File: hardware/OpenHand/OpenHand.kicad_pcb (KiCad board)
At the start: 4 copper layers, 110 x 50 mm, 271 parts, among them J1 CONN_MOTOR_1, J10 CONN_JTAG, J11 CONN_FDBK_2, J12 CONN_EMG_2, J13 CONN_POS_3, J2 CONN_MOTOR_2, J3 CONN_BATT, J4 USB_C_CONN, J5 CONN_POS_1, J6 CONN_MOTOR_3, J7 CONN_FDBK_1, J8 CONN_EMG_1, J9 CONN_POS_2, Q1 2N7002, Q2 2N7002, Q3 PMOS, SW1 SW_Push, SW2 BTN_RST, SW3 BTN_BOOT, U1 CH340C, U10 DRV8833PWP, U11 DRV8833PWP, U12 DRV8833PWP, U13 DRV8833PWP, U14 ESP32-S3-WROOM-1, U2 STM32F103RETx, U3 TPS63070RNMR, U4 AMS1117-3.3, U5 LT1175-5_SOT223, U6 LM324, U7 LM324, U8 ADS1115IDGS, U9 ADS1115IDGS

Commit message: Major updates to schm and pcb, a bit better design
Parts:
- removed the J4 at (104.2, 114.4)
- removed JP17, JP18: SolderJumper_2_Open, Jumper:SolderJumper-2_P1.3mm_Open_RoundedPad1.0x1.5mm
- removed JP19: JMPR_BTN_1, Jumper:SolderJumper-2_P1.3mm_Bridged_RoundedPad1.0x1.5mm
- removed JP20: JMPR_LED_2, Jumper:SolderJumper-2_P1.3mm_Bridged_RoundedPad1.0x1.5mm
- removed JP21: JMPR_BTN_RST, Jumper:SolderJumper-2_P1.3mm_Bridged_RoundedPad1.0x1.5mm
- removed JP22: JMPR_BTN_BOOT, Jumper:SolderJumper-2_P1.3mm_Bridged_RoundedPad1.0x1.5mm
- removed JP23: JMPR_REVP, Jumper:SolderJumper-2_P1.3mm_Bridged_RoundedPad1.0x1.5mm
- removed JP24: JMPR_PSU, Jumper:SolderJumper-2_P1.3mm_Bridged_RoundedPad1.0x1.5mm
- removed JP25: JMPR_EMG_2_UC, Jumper:SolderJumper-2_P1.3mm_Bridged_RoundedPad1.0x1.5mm
- removed JP26: JMPR_EMG_1_UC, Jumper:SolderJumper-2_P1.3mm_Bridged_RoundedPad1.0x1.5mm
- removed JP27: JMPR_I2C_ADC_SCL, Jumper:SolderJumper-2_P1.3mm_Bridged_RoundedPad1.0x1.5mm
- removed JP28: JMPR_I2C_ADC_SDA, Jumper:SolderJumper-2_P1.3mm_Bridged_RoundedPad1.0x1.5mm
- removed JP29: JMPR_MOT_1_EN, Jumper:SolderJumper-2_P1.3mm_Bridged_RoundedPad1.0x1.5mm
- removed JP30: JMPR_MOT_2_EN, Jumper:SolderJumper-2_P1.3mm_Bridged_RoundedPad1.0x1.5mm
- removed JP31: JMPR_MOT_1_UC1, Jumper:SolderJumper-2_P1.3mm_Bridged_RoundedPad1.0x1.5mm
- removed JP32: JMPR_MOT_2_UC1, Jumper:SolderJumper-2_P1.3mm_Bridged_RoundedPad1.0x1.5mm
- removed JP33: JMPR_MOT_1_UC2, Jumper:SolderJumper-2_P1.3mm_Bridged_RoundedPad1.0x1.5mm
- removed JP34: JMPR_MOT_2_UC2, Jumper:SolderJumper-2_P1.3mm_Bridged_RoundedPad1.0x1.5mm
- removed JP35: JMPR_MOT_3_EN, Jumper:SolderJumper-2_P1.3mm_Bridged_RoundedPad1.0x1.5mm
- removed JP36: JMPR_MOT_3_UC1, Jumper:SolderJumper-2_P1.3mm_Bridged_RoundedPad1.0x1.5mm
- removed JP37: JMPR_MOT_3_UC2, Jumper:SolderJumper-2_P1.3mm_Bridged_RoundedPad1.0x1.5mm
- removed JP38: JMPR_ESP_USB_P, Jumper:SolderJumper-2_P1.3mm_Bridged_RoundedPad1.0x1.5mm
- removed JP39: JMPR_ESP_USB_N, Jumper:SolderJumper-2_P1.3mm_Bridged_RoundedPad1.0x1.5mm
- removed JP40: JMPR_ESP_SCL, Jumper:SolderJumper-2_P1.3mm_Bridged_RoundedPad1.0x1.5mm
- removed JP41: JMPR_ESP_SDA, Jumper:SolderJumper-2_P1.3mm_Bridged_RoundedPad1.0x1.5mm
- removed Q2: 2N7002, Package_TO_SOT_SMD:SOT-23
- removed Q3: PMOS, Package_DIP:Vishay_HVM-DIP-3_W7.62mm
- removed R61: 10k, Resistor_SMD:R_1206_3216Metric_Pad1.30x1.75mm_HandSolder
- removed R62, R64: 4R7, Resistor_SMD:R_1206_3216Metric_Pad1.30x1.75mm_HandSolder
- removed R63: 0R2, Resistor_SMD:R_1206_3216Metric_Pad1.30x1.75mm_HandSolder
- removed TP57: TP_MOT_2_IS, TestPoint:TestPoint_Pad_D1.0mm
- removed TP58: TP_MOT_2_FAULT, TestPoint:TestPoint_Pad_D1.0mm
- removed TP59: TP_MOT_1_UC1, TestPoint:TestPoint_Pad_D1.0mm
- removed TP60: TP_MOT_2_UC1, TestPoint:TestPoint_Pad_D1.0mm
- removed TP61: TP_MOT_1_UC2, TestPoint:TestPoint_Pad_D1.0mm
- removed TP62: TP_MOT_2_UC2, TestPoint:TestPoint_Pad_D1.0mm
- removed TP63: TP_MOT_1_OUT_P, TestPoint:TestPoint_Pad_D1.0mm
- removed TP64: TP_MOT_2_OUT_P, TestPoint:TestPoint_Pad_D1.0mm
- removed TP65: TP_MOT_1_OUT_N, TestPoint:TestPoint_Pad_D1.0mm
- removed TP66: TP_MOT_2_OUT_N, TestPoint:TestPoint_Pad_D1.0mm
- removed TP67: TP_MOT_3_EN, TestPoint:TestPoint_Pad_D1.0mm
- removed TP68: TP_FDBK_MOT_EN, TestPoint:TestPoint_Pad_D1.0mm
- removed TP69: TP_MOT_3_IS, TestPoint:TestPoint_Pad_D1.0mm
- removed TP70: TP_MOT_3_FAULT, TestPoint:TestPoint_Pad_D1.0mm
- removed TP71: TP_FDBK_MOT_FAULT, TestPoint:TestPoint_Pad_D1.0mm
- removed TP72: TP_MOT_3_UC1, TestPoint:TestPoint_Pad_D1.0mm
- removed TP73: TP_FDBK_MOT_1_UC1, TestPoint:TestPoint_Pad_D1.0mm
- removed TP74: TP_MOT_3_UC2, TestPoint:TestPoint_Pad_D1.0mm
- removed TP75: TP_FDBK_MOT_1_UC2, TestPoint:TestPoint_Pad_D1.0mm
- removed TP76: TP_MOT_3_OUT_P, TestPoint:TestPoint_Pad_D1.0mm
- removed TP77: TP_MOT_3_OUT_N, TestPoint:TestPoint_Pad_D1.0mm
- removed TP78: TP_FDBK_MOT_2_UC1, TestPoint:TestPoint_Pad_D1.0mm
- removed TP79: TP_FDBK_MOT_2_UC2, TestPoint:TestPoint_Pad_D1.0mm
- removed TP80: TP_ESP_SCL, TestPoint:TestPoint_Pad_D1.0mm
- removed TP81: TP_ESP_SDA, TestPoint:TestPoint_Pad_D1.0mm
- removed U11, U12, U13: DRV8833PWP, Package_SO:HTSSOP-16-1EP_4.4x5mm_P0.65mm_EP3.4x5mm_Mask2.46x2.31mm_ThermalVias
- removed U14: ESP32-S3-WROOM-1, Espressif:ESP32-S3-WROOM-1
- added C39: 10u, Capacitor_SMD:C_0805_2012Metric, F.Cu at (181.2, 122.0)
- added J5: USB_C_CONN, Connector_USB:USB_C_Receptacle_G-Switch_GT-USB-7010ASV, F.Cu at (104.0, 114.1)
- added TP39: TP_MOT_2_UC2, TestPoint:TestPoint_Pad_D1.0mm, B.Cu at (145.9, 117.1)
- added TP40: TP_MOT_1_OUT_P, TestPoint:TestPoint_Pad_D1.0mm, F.Cu at (176.1, 137.7)
- C1: value 1u -> 100n; footprint Capacitor_SMD:C_1206_3216Metric_Pad1.33x1.80mm_HandSolder -> Capacitor_SMD:C_0805_2012Metric
- C10, C5, C9: value 10u -> 100n; footprint Capacitor_SMD:C_0805_2012Metric_Pad1.18x1.45mm_HandSolder -> Capacitor_SMD:C_0805_2012Metric
- C11: value 10u -> 22u; footprint Capacitor_SMD:C_0805_2012Metric_Pad1.18x1.45mm_HandSolder -> Capacitor_SMD:C_0805_2012Metric
- C12, C15: value 100n -> 22u; footprint Capacitor_SMD:C_1206_3216Metric_Pad1.33x1.80mm_HandSolder -> Capacitor_SMD:C_0805_2012Metric
- C13: value 22u -> 1u; footprint Capacitor_SMD:C_0805_2012Metric_Pad1.18x1.45mm_HandSolder -> Capacitor_SMD:C_0805_2012Metric
- C14, C18, C19, C20, C21, C22, C24, C26, C28, C30, C32, C34, C36, C38: footprint Capacitor_SMD:C_0805_2012Metric_Pad1.18x1.45mm_HandSolder -> Capacitor_SMD:C_0805_2012Metric
- C16, C2, C3, C4: footprint Capacitor_SMD:C_1206_3216Metric_Pad1.33x1.80mm_HandSolder -> Capacitor_SMD:C_0805_2012Metric
- C17: value 470n -> 100n; footprint Capacitor_SMD:C_0805_2012Metric_Pad1.18x1.45mm_HandSolder -> Capacitor_SMD:C_0805_2012Metric
- C23: value 330n -> 470n; footprint Capacitor_SMD:C_0805_2012Metric_Pad1.18x1.45mm_HandSolder -> Capacitor_SMD:C_0805_2012Metric
- C25: value 10u -> 330n; footprint Capacitor_SMD:C_0805_2012Metric_Pad1.18x1.45mm_HandSolder -> Capacitor_SMD:C_0805_2012Metric
- C27, C33: value 2u2 -> 10u; footprint Capacitor_SMD:C_0805_2012Metric_Pad1.18x1.45mm_HandSolder -> Capacitor_SMD:C_0805_2012Metric
- C29, C35: value 10n -> 2u2; footprint Capacitor_SMD:C_0805_2012Metric_Pad1.18x1.45mm_HandSolder -> Capacitor_SMD:C_0805_2012Metric
- C31, C37: value 10u -> 10n; footprint Capacitor_SMD:C_0805_2012Metric_Pad1.18x1.45mm_HandSolder -> Capacitor_SMD:C_0805_2012Metric
- C6: value 22u -> 100n; footprint Capacitor_SMD:C_0805_2012Metric_Pad1.18x1.45mm_HandSolder -> Capacitor_SMD:C_0805_2012Metric
- C7, C8: value 22u -> 10u; footprint Capacitor_SMD:C_0805_2012Metric_Pad1.18x1.45mm_HandSolder -> Capacitor_SMD:C_0805_2012Metric
- D1, D2, D4: footprint LED_SMD:LED_0805_2012Metric -> LED_SMD:LED_1210_3225Metric
- D3: footprint Diode_THT:D_A-405_P7.62mm_Horizontal -> Diode_SMD:D_SOD-123
- JP1: value JMPR_RST -> JMPR_TRIM_1
- JP14: value JMPR_LED_1 -> SolderJumper_2_Open; footprint Jumper:SolderJumper-2_P1.3mm_Bridged_RoundedPad1.0x1.5mm -> Jumper:SolderJumper-2_P1.3mm_Open_RoundedPad1.0x1.5mm; moved to B.Cu
- JP15: value SolderJumper_2_Open -> JMPR_EMG_1_UC; footprint Jumper:SolderJumper-2_P1.3mm_Open_RoundedPad1.0x1.5mm -> Jumper:SolderJumper-2_P1.3mm_Bridged_RoundedPad1.0x1.5mm; moved to F.Cu
- JP16: value SolderJumper_2_Open -> JMPR_EMG_2_UC; footprint Jumper:SolderJumper-2_P1.3mm_Open_RoundedPad1.0x1.5mm -> Jumper:SolderJumper-2_P1.3mm_Bridged_RoundedPad1.0x1.5mm; moved to F.Cu
- JP2: value JMPR_RX -> JMPR_LED_1
- JP3: value JMPR_TX -> JMPR_BTN_1
- JP4: value JMPR_USB_P -> JMPR_LED_2
- JP5: value JMPR_USB_N -> JMPR_TRIM_2
- JP6: value JMPR_BOOT -> JMPR_POT_1
- JP7: value JMPR_POT_1 -> SolderJumper_2_Open; footprint Jumper:SolderJumper-2_P1.3mm_Bridged_RoundedPad1.0x1.5mm -> Jumper:SolderJumper-2_P1.3mm_Open_RoundedPad1.0x1.5mm; moved to B.Cu
- JP8: value JMPR_TRIM_1 -> SolderJumper_2_Open; footprint Jumper:SolderJumper-2_P1.3mm_Bridged_RoundedPad1.0x1.5mm -> Jumper:SolderJumper-2_P1.3mm_Open_RoundedPad1.0x1.5mm; moved to B.Cu
- JP9: value JMPR_TRIM_2 -> SolderJumper_2_Open; footprint Jumper:SolderJumper-2_P1.3mm_Bridged_RoundedPad1.0x1.5mm -> Jumper:SolderJumper-2_P1.3mm_Open_RoundedPad1.0x1.5mm; moved to B.Cu
- L1: value 1.5uH -> 3.3uH; footprint Inductor_THT:L_Radial_D6.0mm_P4.00mm -> Inductor_SMD:L_Bourns_SRP7028A_7.3x6.6mm
- Q1: value 2N7002 -> AO3401A
- R1: value 5k1 -> 10k; footprint Resistor_SMD:R_0805_2012Metric_Pad1.20x1.40mm_HandSolder -> Resistor_SMD:R_0805_2012Metric
- R10, R9: value 10k -> 4k7; footprint Resistor_SMD:R_0805_2012Metric_Pad1.20x1.40mm_HandSolder -> Resistor_SMD:R_0805_2012Metric; moved to F.Cu
- R11: value 4k7 -> 47k; footprint Resistor_SMD:R_0805_2012Metric_Pad1.20x1.40mm_HandSolder -> Resistor_SMD:R_0805_2012Metric
- R12, R19, R2, R22, R25, R26, R27, R28, R29, R30, R31, R32, R33, R37, R38, R39, R40, R41, R42, R45, R46, R47, R48, R49, R5, R50, R51, R52, R53, R6: footprint Resistor_SMD:R_0805_2012Metric_Pad1.20x1.40mm_HandSolder -> Resistor_SMD:R_0805_2012Metric
- R13: value 4k7 -> 10k; footprint Resistor_SMD:R_0805_2012Metric_Pad1.20x1.40mm_HandSolder -> Resistor_SMD:R_0805_2012Metric; moved to B.Cu
- R14, R15, R16: footprint Resistor_SMD:R_0805_2012Metric_Pad1.20x1.40mm_HandSolder -> Resistor_SMD:R_0805_2012Metric; moved to B.Cu
- R17: value 680k -> 10k; footprint Resistor_SMD:R_0805_2012Metric_Pad1.20x1.40mm_HandSolder -> Resistor_SMD:R_0805_2012Metric
- R18: value 100k -> 54.9k; footprint Resistor_SMD:R_0805_2012Metric_Pad1.20x1.40mm_HandSolder -> Resistor_SMD:R_0805_2012Metric
- R20: value 130k -> 4k7; footprint Resistor_SMD:R_0805_2012Metric_Pad1.20x1.40mm_HandSolder -> Resistor_SMD:R_0805_2012Metric
- R21: value 4k7 -> 10k; footprint Resistor_SMD:R_0805_2012Metric_Pad1.20x1.40mm_HandSolder -> Resistor_SMD:R_0805_2012Metric
- R23: value 47k -> 15k; footprint Resistor_SMD:R_0805_2012Metric_Pad1.20x1.40mm_HandSolder -> Resistor_SMD:R_0805_2012Metric
- R24, R35: value 15k -> 47k; footprint Resistor_SMD:R_0805_2012Metric_Pad1.20x1.40mm_HandSolder -> Resistor_SMD:R_0805_2012Metric
- R3: value 1k -> 5k1; footprint Resistor_SMD:R_0805_2012Metric_Pad1.20x1.40mm_HandSolder -> Resistor_SMD:R_0805_2012Metric
- R34: value 47k -> 10k; footprint Resistor_SMD:R_0805_2012Metric_Pad1.20x1.40mm_HandSolder -> Resistor_SMD:R_0805_2012Metric
- R36: value 10k -> 15k; footprint Resistor_SMD:R_0805_2012Metric_Pad1.20x1.40mm_HandSolder -> Resistor_SMD:R_0805_2012Metric
- R4: value 1k -> 1.5k; footprint Resistor_SMD:R_0805_2012Metric_Pad1.20x1.40mm_HandSolder -> Resistor_SMD:R_0805_2012Metric
- R43: value 1k -> 47k; footprint Resistor_SMD:R_0805_2012Metric_Pad1.20x1.40mm_HandSolder -> Resistor_SMD:R_0805_2012Metric
- R44: value 47k -> 1k; footprint Resistor_SMD:R_0805_2012Metric_Pad1.20x1.40mm_HandSolder -> Resistor_SMD:R_0805_2012Metric
- R54: value 47k -> 0R2; footprint Resistor_SMD:R_0805_2012Metric_Pad1.20x1.40mm_HandSolder -> Resistor_SMD:R_1206_3216Metric
- R55: value 10k -> 0R2; footprint Resistor_SMD:R_0805_2012Metric_Pad1.20x1.40mm_HandSolder -> Resistor_SMD:R_1206_3216Metric
- R56, R57: footprint Resistor_SMD:R_1206_3216Metric_Pad1.30x1.75mm_HandSolder -> Resistor_SMD:R_0805_2012Metric
- R58: value 0R2 -> 4R7; footprint Resistor_SMD:R_1206_3216Metric_Pad1.30x1.75mm_HandSolder -> Resistor_SMD:R_1206_3216Metric
- R59: footprint Resistor_SMD:R_1206_3216Metric_Pad1.30x1.75mm_HandSolder -> Resistor_SMD:R_1206_3216Metric
- R60: value 10k -> 4R7; footprint Resistor_SMD:R_1206_3216Metric_Pad1.30x1.75mm_HandSolder -> Resistor_SMD:R_1206_3216Metric
- R7, R8: footprint Resistor_SMD:R_0805_2012Metric_Pad1.20x1.40mm_HandSolder -> Resistor_SMD:R_0805_2012Metric; moved to F.Cu
- RV1: value TRIM_POT_3 -> TRIM_POT_1
- RV2: value TRIM_POT_1 -> TRIM_POT_2
- RV3: value TRIM_POT_2 -> TRIM_POT_3
- SW1: value SW_Push -> BTN_RST
- SW2: value BTN_RST -> BTN_BOOT
- SW3: value BTN_BOOT -> SW_Push
- TP1: value TP_UC_RST -> TP_BTN_RST
- TP10: value TP_UC_RX -> TP_HALL_01
- TP11: value TP_LED_1 -> TP_HALL_02
- TP12: value TP_UC_TX -> TP_HALL_03
- TP13: value TP_HW_REV_3 -> TP_UC_TX; moved to F.Cu
- TP14: value TP_UC_PIN_PD1 -> TP_UC_RX; moved to F.Cu
- TP15: value TP_HW_REV_4 -> TP_UC_PIN_PC12; moved to F.Cu
- TP16: value TP_UC_PIN_PD2 -> TP_UC_SCL; moved to F.Cu
- TP17: value TP_UC_PIN_PC0 -> TP_UC_SDA; moved to F.Cu
- TP18: value TP_UC_PIN_PC1 -> TP_UC_PIN_PB12; moved to F.Cu
- TP19: value TP_LED_2 -> TP_BATT_P
- TP20: value TP_UC_PIN_PC2 -> TP_V_BATT; moved to F.Cu
- TP21: value TP_UC_PIN_PC3 -> TP_V_5V; moved to F.Cu
- TP22: value TP_UC_PIN_PB2 -> TP_V_3V3; moved to F.Cu
- TP23: value TP_UC_PIN_PC13 -> TP_V_N5V; moved to F.Cu
- TP24: value TP_UC_PIN_PB5 -> TP_EMG_1_AMP; moved to F.Cu
- TP25: value TP_UC_PIN_PC14 -> TP_EMG_2_AMP; moved to F.Cu
- TP26: value TP_UC_PIN_PC15 -> TP_EMG_1_HP; moved to F.Cu
- TP27: value TP_UC_PIN_PB10 -> TP_EMG_2_HP; moved to F.Cu
- TP28: value TP_UC_PIN_PB11 -> TP_EMG_1_LP; moved to F.Cu
- TP29: value TP_BATT_P -> TP_EMG_2_LP
- TP30: value TP_V_BATT -> TP_MOT_1_EN
- TP31: value TP_V_5V -> TP_MOT_2_EN
- TP32: value TP_PSU_FDBK -> TP_MOT_1_IS
- TP33: value TP_V_3V3 -> TP_MOT_1_FAULT
- TP34: value TP_V_N5V -> TP_MOT_2_IS
- TP35: value TP_EMG_2_AMP -> TP_MOT_2_FAULT
- TP36: value TP_EMG_1_AMP -> TP_MOT_1_UC1; moved to B.Cu
- TP37: value TP_EMG_2_HP -> TP_MOT_2_UC1; moved to B.Cu
- TP38: value TP_EMG_1_HP -> TP_MOT_1_UC2; moved to B.Cu
- TP4: value TP_UC_BOOT -> TP_BTN_BOOT
- TP41: value TP_EMG_2_LP -> TP_MOT_2_OUT_P
- TP42: value TP_EMG_1_LP -> TP_MOT_1_OUT_N
- TP43: value TP_ADC_RDY -> TP_MOT_2_OUT_N
- TP44: value TP_TRIM_1 -> TP_MOT_3_EN
- TP45: value TP_TRIM_2 -> TP_FDBK_MOT_EN
- TP46: value TP_TRIM_3 -> TP_MOT_3_IS
- TP47: value TP_TRIM_4 -> TP_MOT_3_FAULT
- TP48: value TP_ADC_RDY -> TP_FDBK_MOT_FAULT
- TP49: value TP_BATT_SENSE -> TP_MOT_3_UC1; moved to B.Cu
- TP5: value TP_UC_SCL -> TP_UC_PIN_PD1
- TP50: value TP_HALL_01 -> TP_FDBK_MOT_1_UC1; moved to B.Cu
- TP51: value TP_HALL_02 -> TP_MOT_3_UC2; moved to B.Cu
- TP52: value TP_HALL_03 -> TP_FDBK_MOT_1_UC2; moved to B.Cu
- TP53: value TP_MOT_1_EN -> TP_MOT_3_OUT_P; moved to F.Cu
- TP54: value TP_MOT_2_EN -> TP_MOT_3_OUT_N; moved to F.Cu
- TP55: value TP_MOT_1_IS -> TP_FDBK_MOT_2_UC1; moved to B.Cu
- TP56: value TP_MOT_1_FAULT -> TP_FDBK_MOT_2_UC2; moved to B.Cu
- TP6: value TP_UC_SDA -> TP_UC_PIN_PA5
- TP7: value TP_HW_REV_1 -> TP_UC_PIN_PD2; moved to F.Cu
- TP8: value TP_HW_REV_2 -> TP_UC_PIN_PA6; moved to F.Cu
- TP9: value TP_UC_PIN_PD0 -> TP_BATT_SENSE; moved to F.Cu
- U1: value CH340C -> STM32F103RETx; footprint Package_SO:SOIC-16_3.9x9.9mm_P1.27mm -> Package_QFP:LQFP-64_10x10mm_P0.5mm
- U2: value STM32F103RETx -> TPS565201DDCR; footprint Package_QFP:LQFP-64_10x10mm_P0.5mm -> TPS565201DDCR:TPS565201DDCR_L
- U3: value TPS63070RNMR -> AMS1117-3.3; footprint TPS63070RNMR:TPS63070RNMR -> Package_TO_SOT_SMD:SOT-223-3_TabPin2
- U4: value AMS1117-3.3 -> LT1175-5_SOT223
- U5: value LT1175-5_SOT223 -> LM324; footprint Package_TO_SOT_SMD:SOT-223-3_TabPin2 -> Package_SO:SO-14_5.3x10.2mm_P1.27mm
- U7: value LM324 -> DRV8833PWP; footprint Package_SO:SO-14_5.3x10.2mm_P1.27mm -> Package_SO:HTSSOP-16-1EP_4.4x5mm_P0.65mm_EP3.4x5mm_Mask2.46x2.31mm_ThermalVias
- U8, U9: value ADS1115IDGS -> DRV8833PWP; footprint Package_SO:TSSOP-10_3x3mm_P0.5mm -> Package_SO:HTSSOP-16-1EP_4.4x5mm_P0.65mm_EP3.4x5mm_Mask2.46x2.31mm_ThermalVias
- moved C15 122.3 mm to (104.6, 130.8)
- moved TP24 92.4 mm to (165.7, 114.4), turned to 0 degrees
- moved TP33 91.8 mm to (193.7, 127.2)
- moved TP26 90.3 mm to (158.6, 132.4), turned to 0 degrees
- moved TP28 83.0 mm to (158.6, 130.2)
- moved TP34 82.1 mm to (195.2, 133.6)
- moved C23 81.8 mm to (142.7, 131.3), turned to 90 degrees
- moved TP35 81.2 mm to (201.9, 127.2)
- moved TP25 80.5 mm to (147.2, 114.2), turned to 0 degrees
- moved TP30 78.1 mm to (185.4, 124.8)
- moved C25 76.7 mm to (146.9, 131.3), turned to 90 degrees
- moved TP14 76.2 mm to (138.3, 107.9), turned to 0 degrees
- moved TP41 75.1 mm to (184.9, 137.7), turned to 90 degrees
- moved C17 73.9 mm to (142.2, 121.4), turned to 90 degrees
- moved C22 73.4 mm to (160.9, 131.6), turned to 90 degrees
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- renumbered J5 to J4
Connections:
- C1 pad 1: +5V -> UC_RST
- C10 pad 1: +BATT -> Net-(U2-SW)
- C10 pad 2: Earth -> Net-(U2-VBST)
- C11 pad 1: +BATT -> +5V
- C12 pad 1: Net-(U3-VAUX) -> +5V
- C13 pad 1: +3V3 -> +5V
- C14 pad 1: -5V -> +3V3
- C15 pad 1: +5V -> -5V
- C17 pad 1: Net-(C17-Pad1) -> +5V
- C17 pad 2: Net-(C17-Pad2) -> Earth
- C18 pad 1: Net-(C17-Pad2) -> Net-(C18-Pad1)
- C18 pad 2: Net-(U7B-+) -> Net-(C18-Pad2)
- C19 pad 1: Net-(C19-Pad1) -> Net-(C18-Pad2)
- C19 pad 2: Net-(C19-Pad2) -> Net-(U5B-+)
- C2 pad 1: Net-(U1-V3) -> UC_BOOT
- C20 pad 1: Net-(C19-Pad2) -> Net-(C20-Pad1)
- C20 pad 2: Net-(U6B-+) -> Net-(C20-Pad2)
- C21 pad 1: EMG_2_MIDPOINT -> Net-(C20-Pad2)
- C21 pad 2: Net-(U7D-+) -> Net-(U6B-+)
- C22 pad 2: Net-(U6D-+) -> Net-(U5D-+)
- C23 pad 1: Earth -> EMG_2_MIDPOINT
- C23 pad 2: Net-(U7C-+) -> Net-(U6D-+)
- C24 pad 2: Net-(U6C-+) -> Net-(U5C-+)
- C25 pad 1: Net-(D6-K) -> Earth
- C25 pad 2: Earth -> Net-(U6C-+)
- C27 pad 1: Earth -> Net-(D6-K)
- C27 pad 2: Net-(U10-VINT) -> Earth
- C28 pad 2: Net-(U11-VINT) -> Net-(U7-VINT)
- C29 pad 1: +5V -> Earth
- C29 pad 2: Net-(U10-VCP) -> Net-(U8-VINT)
- C3 pad 1: UC_RST -> +3V3
- C30 pad 2: Net-(U11-VCP) -> Net-(U7-VCP)
- C31 pad 2: Earth -> Net-(U8-VCP)
- C33 pad 1: Earth -> +5V
- C33 pad 2: Net-(U12-VINT) -> Earth
- C34 pad 2: Net-(U13-VINT) -> Net-(U9-VINT)
- C35 pad 1: +5V -> Earth
- C35 pad 2: Net-(U12-VCP) -> Net-(U10-VINT)
- C36 pad 2: Net-(U13-VCP) -> Net-(U9-VCP)
- C37 pad 2: Earth -> Net-(U10-VCP)
- C4 pad 1: UC_BOOT -> +3V3
- C5 pad 1: Net-(JP24-A) -> +3V3
- C6 pad 1: +5V -> +3V3
- C7 pad 1: +5V -> +BATT
- C8 pad 1: +5V -> +BATT
- J1 pad 1: MOTOR_1_N -> MOTOR_01_N
- J1 pad 2: MOTOR_1_P -> MOTOR_01_P
- J11 pad 1: FDBK_MOTOR_2_N -> HAPTIC_02_N
- J11 pad 2: FDBK_MOTOR_2_P -> HAPTIC_02_P
- J12 pad 2: EMG_2_N -> EMG_02_P
- J12 pad 3: EMG_2_P -> EMG_02_N
- J2 pad 1: MOTOR_2_N -> MOTOR_02_N
- J2 pad 2: MOTOR_2_P -> MOTOR_02_P
- J6 pad 1: MOTOR_3_N -> MOTOR_03_N
- J6 pad 2: MOTOR_3_P -> MOTOR_03_P
- J7 pad 1: FDBK_MOTOR_1_N -> HAPTIC_01_N
- J7 pad 2: FDBK_MOTOR_1_P -> HAPTIC_01_P
- J8 pad 2: EMG_1_N -> EMG_01_P
- J8 pad 3: EMG_1_P -> EMG_01_N
- JP1 pad 2: UC_RST -> TRIM_POT_01
- JP10 pad 1: HW_REV_1 -> HW_REV_04
- JP11 pad 1: HW_REV_2 -> Earth
- JP11 pad 2: Net-(JP11-B) -> HW_REV_01
- JP12 pad 1: HW_REV_3 -> Earth
- JP12 pad 2: Net-(JP12-B) -> HW_REV_02
- JP13 pad 1: HW_REV_4 -> Earth
- JP13 pad 2: Net-(JP13-B) -> HW_REV_03
- JP14 pad 1: Net-(D1-A) -> Earth
- JP14 pad 2: LED_1 -> HW_REV_04
- JP15 pad 1: Earth -> Net-(D5-K)
- JP15 pad 2: HW_REV_1 -> EMG_01_UC
- JP16 pad 1: Earth -> Net-(D6-K)
- JP16 pad 2: HW_REV_2 -> EMG_02_UC
- JP2 pad 1: Net-(JP2-A) -> Net-(D1-A)
- JP2 pad 2: UC_RX -> LED_1
- JP3 pad 1: UC_TX -> Net-(JP3-A)
- JP3 pad 2: Net-(JP3-B) -> BTN_01
- JP4 pad 1: USB_D_P -> Net-(D2-A)
- JP4 pad 2: Net-(JP4-B) -> LED_2
- JP5 pad 2: USB_D_N -> TRIM_POT_02
- JP6 pad 2: UC_BOOT -> TRIM_POT_03
- JP7 pad 1: Net-(JP7-A) -> HW_REV_01
- JP7 pad 2: TRIM_POT_3 -> Net-(JP7-B)
- JP8 pad 1: Net-(JP8-A) -> HW_REV_02
- JP8 pad 2: TRIM_POT_1 -> Net-(JP8-B)
- JP9 pad 1: Net-(JP9-A) -> HW_REV_03
- JP9 pad 2: TRIM_POT_2 -> Net-(JP9-B)
- L1 pad 1: Net-(U3-L1) -> Net-(U2-SW)
- L1 pad 2: Net-(U3-L2) -> +5V
- Q1 pad 1: Net-(Q1-G) -> Net-(D3-A)
- Q1 pad 2: Net-(Q1-S) -> +BATT
- Q1 pad 3: Net-(JP1-A) -> BAT_P
- R1 pad 1: Net-(J4-CC1) -> +3V3
- R1 pad 2: Earth -> UC_RST
- R10 pad 1: +3V3 -> Net-(D2-K)
- R10 pad 2: Net-(JP13-B) -> Earth
- R11 pad 1: Net-(D1-K) -> Net-(U1-PC0)
- R11 pad 2: Earth -> +BATT
- R12 pad 1: +3V3 -> Earth
- R12 pad 2: Net-(JP19-A) -> Net-(U1-PC0)
- R13 pad 1: Net-(D2-K) -> +3V3
- R13 pad 2: Earth -> Net-(JP7-B)
- R14 pad 2: Net-(JP21-A) -> Net-(JP8-B)
- R15 pad 2: Net-(JP22-A) -> Net-(JP9-B)
- R16 pad 1: Net-(U3-EN) -> +3V3
- R16 pad 2: Net-(JP23-B) -> Net-(JP10-B)
- R17 pad 1: Net-(U3-FB) -> Net-(U2-EN)
- R17 pad 2: Net-(JP24-A) -> +BATT
- R18 pad 1: Net-(U3-PG) -> +5V
- R18 pad 2: Net-(JP24-A) -> Net-(U2-VFB)
- R20 pad 1: Earth -> Net-(D4-K)
- R20 pad 2: Net-(U3-FB) -> Earth
- R21 pad 1: Net-(D4-K) -> Net-(U2-VFB)
- R22 pad 2: Net-(U7A-+) -> Net-(U5A-+)
- R23 pad 1: Earth -> Net-(C18-Pad2)
- R23 pad 2: Net-(U6A-+) -> Net-(R23-Pad2)
- R24 pad 1: Net-(C17-Pad2) -> Earth
- R24 pad 2: Net-(R24-Pad2) -> Net-(U6A-+)
- R25 pad 1: Net-(C19-Pad2) -> Net-(C20-Pad2)
- R26 pad 1: Net-(U7A-+) -> Net-(U5A-+)
- R26 pad 2: EMG_2_P -> EMG_01_P
- R27 pad 2: EMG_1_P -> EMG_02_P
- R28 pad 1: Net-(U7A--) -> Net-(U5A--)
- R28 pad 2: EMG_2_N -> EMG_01_N
- R29 pad 1: Net-(R24-Pad2) -> Net-(R23-Pad2)
- R29 pad 2: EMG_2_MIDPOINT -> EMG_1_MIDPOINT
- R3 pad 1: Net-(Q2-S) -> Net-(J5-CC2)
- R3 pad 2: Net-(Q1-G) -> Earth
- R30 pad 2: EMG_1_N -> EMG_02_N
- R31 pad 2: EMG_1_MIDPOINT -> EMG_2_MIDPOINT
- R32 pad 1: Net-(U7A--) -> Net-(U5A--)
- R32 pad 2: Net-(C17-Pad1) -> Net-(C18-Pad1)
- R33 pad 1: Net-(U7B-+) -> Net-(U5B-+)
- R34 pad 1: Net-(U6A--) -> Net-(U5B--)
- R34 pad 2: Net-(C19-Pad1) -> Net-(R23-Pad2)
- R35 pad 1: Net-(U6B-+) -> Net-(U6A--)
- R35 pad 2: Earth -> Net-(C20-Pad1)
- R36 pad 1: Net-(U7B--) -> Net-(U6B-+)
- R36 pad 2: Net-(R24-Pad2) -> Earth
- R38 pad 1: Net-(U7B--) -> Net-(U5B--)
- R4 pad 1: Net-(Q1-S) -> USB_D+
- R4 pad 2: Net-(Q2-G) -> +3V3
- R40 pad 1: EMG_2_MIDPOINT -> EMG_1_MIDPOINT
- R40 pad 2: Net-(U7C-+) -> Net-(U5C-+)
- R41 pad 1: EMG_1_MIDPOINT -> EMG_2_MIDPOINT
- R42 pad 1: Net-(D5-A) -> Net-(D6-A)
- R43 pad 1: Net-(U7D--) -> Net-(D5-A)
- R43 pad 2: Earth -> Net-(R43-Pad2)
- R44 pad 1: Net-(D6-A) -> Net-(U5D--)
- R44 pad 2: Net-(R44-Pad2) -> Earth
- R46 pad 1: Net-(U7C--) -> Net-(U5C--)
- R46 pad 2: Net-(U7D-+) -> Net-(U5D-+)
- R48 pad 1: Net-(D6-K) -> Net-(D5-K)
- R49 pad 1: Net-(U7C--) -> Net-(U5C--)
- R5 pad 1: UC_SDA -> +3V3
- R5 pad 2: +3V3 -> UC_BOOT
- R50 pad 1: Net-(D5-K) -> Net-(U6C--)
- R51 pad 1: Net-(U6C--) -> Net-(D6-K)
- R52 pad 1: ADC_2_ALERT_RDY -> MOTOR_01_EN
- R52 pad 2: +3V3 -> +5V
- R53 pad 1: ADC_1_ALERT_RDY -> MOTOR_02_EN
- R53 pad 2: +3V3 -> +5V
- R54 pad 1: Net-(U9-AIN0) -> Earth
- R54 pad 2: +BATT -> Net-(U7-AISEN)
- R55 pad 2: Net-(U9-AIN0) -> Net-(U8-AISEN)
- R56 pad 1: Net-(JP29-B) -> MOTOR_03_EN
- R57 pad 1: Net-(JP30-B) -> HAPTIC_EN
- R59 pad 2: Net-(U11-AISEN) -> Net-(U9-AISEN)
- R6 pad 1: UC_SCL -> UC_SDA
- R60 pad 1: Net-(JP35-B) -> Earth
- R60 pad 2: +5V -> Net-(U10-BISEN)
- R7 pad 1: +3V3 -> UC_SCL
- R7 pad 2: Net-(JP10-B) -> +3V3
- R8 pad 2: Net-(JP11-B) -> Net-(JP3-A)
- R9 pad 1: +3V3 -> Net-(D1-K)
- R9 pad 2: Net-(JP12-B) -> Earth
- RV1 pad 2: Net-(JP7-A) -> Net-(JP1-A)
- RV2 pad 2: Net-(JP8-A) -> Net-(JP5-A)
- RV3 pad 2: Net-(JP9-A) -> Net-(JP6-A)
- RV4 pad 1: Net-(R42-Pad2) -> Net-(R43-Pad2)
- RV4 pad 2: Net-(R42-Pad2) -> Net-(R43-Pad2)
- RV4 pad 3: Net-(U7D--) -> Net-(U5D--)
- RV5 pad 1: Net-(R44-Pad2) -> Net-(R42-Pad2)
- RV5 pad 2: Net-(R44-Pad2) -> Net-(R42-Pad2)
- SW1 pad 1: Net-(JP19-A) -> UC_RST
- SW2 pad 1: Net-(JP21-A) -> UC_BOOT
- SW3 pad 1: Net-(JP22-A) -> Net-(JP3-A)
- TP10 pad 1: UC_RX -> HALL_SENS_01_S
- TP11 pad 1: Net-(D1-A) -> HALL_SENS_02_S
- TP12 pad 1: UC_TX -> HALL_SENS_03_S
- TP13 pad 1: HW_REV_3 -> UC_TX
- TP14 pad 1: Net-(U2-PD1) -> UC_RX
- TP15 pad 1: HW_REV_4 -> Net-(U1-PC12)
- TP16 pad 1: Net-(U2-PD2) -> UC_SCL
- TP17 pad 1: Net-(U2-PC0) -> UC_SDA
- TP18 pad 1: Net-(U2-PC1) -> Net-(U1-PB12)
- TP19 pad 1: Net-(D2-A) -> BAT_P
- TP2 pad 1: USB_D_P -> USB_D+
- TP20 pad 1: Net-(U2-PC2) -> +BATT
- TP21 pad 1: Net-(U2-PC3) -> +5V
- TP22 pad 1: Net-(U2-PB2) -> +3V3
- TP23 pad 1: Net-(U2-PC13) -> -5V
- TP24 pad 1: Net-(U2-PB5) -> Net-(C18-Pad1)
- TP25 pad 1: Net-(U2-PC14) -> Net-(C20-Pad1)
- TP26 pad 1: Net-(U2-PC15) -> EMG_1_MIDPOINT
- TP27 pad 1: Net-(U2-PB10) -> EMG_2_MIDPOINT
- TP28 pad 1: Net-(U2-PB11) -> Net-(U5D-+)
- TP29 pad 1: BAT_P -> Net-(U6D-+)
- TP3 pad 1: USB_D_N -> USB_D-
- TP30 pad 1: +BATT -> MOTOR_01_EN
- TP31 pad 1: +5V -> MOTOR_02_EN
- TP32 pad 1: Net-(U3-FB) -> Net-(U7-AISEN)
- TP33 pad 1: +3V3 -> MOTOR_01_FAULT
- TP34 pad 1: -5V -> Net-(U8-AISEN)
- TP35 pad 1: Net-(C17-Pad1) -> MOTOR_02_FAULT
- TP36 pad 1: Net-(C19-Pad1) -> MOTOR_01_DIR
- TP37 pad 1: EMG_2_MIDPOINT -> MOTOR_02_DIR
- TP38 pad 1: EMG_1_MIDPOINT -> MOTOR_01_PWM
- TP41 pad 1: Net-(U7D-+) -> MOTOR_02_P
- TP42 pad 1: Net-(U6D-+) -> MOTOR_01_N
- TP43 pad 1: ADC_2_ALERT_RDY -> MOTOR_02_N
- TP44 pad 1: TRIM_POT_1 -> MOTOR_03_EN
- TP45 pad 1: TRIM_POT_2 -> HAPTIC_EN
- TP46 pad 1: TRIM_POT_3 -> Net-(U9-AISEN)
- TP47 pad 1: BTN_1 -> MOTOR_03_FAULT
- TP48 pad 1: ADC_1_ALERT_RDY -> HAPTIC_FAULT
- TP49 pad 1: Net-(U9-AIN0) -> MOTOR_03_DIR
- TP5 pad 1: UC_SCL -> Net-(U1-PD1)
- TP50 pad 1: HALL_SENS_01_S -> HAPTIC_01_DIR
- TP51 pad 1: HALL_SENS_02_S -> MOTOR_03_PWM
- TP52 pad 1: HALL_SENS_03_S -> HAPTIC_01_PWM
- TP53 pad 1: MOTOR_1_EN -> MOTOR_03_P
- TP54 pad 1: MOTOR_2_EN -> MOTOR_03_N
- TP55 pad 1: Net-(U10-AISEN) -> HAPTIC_02_DIR
- TP56 pad 1: MOTOR_1_FAULT -> HAPTIC_02_PWM
- TP6 pad 1: UC_SDA -> Net-(U1-PA5)
- TP7 pad 1: HW_REV_1 -> Net-(U1-PD2)
- TP8 pad 1: HW_REV_2 -> Net-(U1-PA6)
- TP9 pad 1: Net-(U2-PD0) -> Net-(U1-PC0)
- U1 pad 1: Earth -> +3V3
- U1 pad 10: unconnected-(U1-~{DSR}-Pad10) -> HALL_SENS_02_S
- U1 pad 11: unconnected-(U1-~{RI}-Pad11) -> HALL_SENS_03_S
- U1 pad 12: unconnected-(U1-~{DCD}-Pad12) -> Earth
- U1 pad 13: Net-(Q2-S) -> +3V3
- U1 pad 14: Net-(Q1-S) -> TRIM_POT_01
- U1 pad 15: unconnected-(U1-R232-Pad15) -> TRIM_POT_02
- U1 pad 16: +5V -> TRIM_POT_03
- U1 pad 2: Net-(JP2-A) -> HW_REV_01
- U1 pad 3: Net-(JP3-B) -> HW_REV_02
- U1 pad 4: Net-(U1-V3) -> HW_REV_03
- U1 pad 5: Net-(JP4-B) -> HW_REV_04
- U1 pad 6: Net-(JP5-A) -> Net-(U1-PD1)
- U1 pad 7: unconnected-(U1-NC-Pad7) -> UC_RST
- U1 pad 8: unconnected-(U1-NC-Pad8) -> Net-(U1-PC0)
- U1 pad 9: unconnected-(U1-~{CTS}-Pad9) -> HALL_SENS_01_S
- U10 pad 1: Net-(JP29-B) -> HAPTIC_EN
- U10 pad 10: Net-(JP33-A) -> HAPTIC_02_PWM
- U10 pad 15: Net-(JP33-A) -> HAPTIC_01_PWM
- U10 pad 16: Net-(JP31-B) -> HAPTIC_01_DIR
- U10 pad 2: MOTOR_1_P -> HAPTIC_01_P
- U10 pad 4: MOTOR_1_N -> HAPTIC_01_N
- U10 pad 5: MOTOR_1_N -> HAPTIC_02_N
- U10 pad 6: Net-(U10-AISEN) -> Net-(U10-BISEN)
- U10 pad 7: MOTOR_1_P -> HAPTIC_02_P
- U10 pad 8: MOTOR_1_FAULT -> HAPTIC_FAULT
- U10 pad 9: Net-(JP31-B) -> HAPTIC_02_DIR
- U2 pad 1: +3V3 -> Earth
- U2 pad 2: Net-(U2-PC13) -> Net-(U2-SW)
- U2 pad 3: Net-(U2-PC14) -> +BATT
- U2 pad 4: Net-(U2-PC15) -> Net-(U2-VFB)
- U2 pad 5: Net-(U2-PD0) -> Net-(U2-EN)
- U2 pad 6: Net-(U2-PD1) -> Net-(U2-VBST)
- U3 pad 1: Net-(U3-EN) -> Earth
- U3 pad 2: Net-(U3-PG) -> +3V3
- U3 pad 3: Net-(U3-VAUX) -> +5V
- U4 pad 1: Earth -> -5V
- U4 pad 2: +3V3 -> +BATT
- U4 pad 3: +5V -> Earth
- U5 pad 1: -5V -> Net-(C18-Pad1)
- U5 pad 2: +BATT -> Net-(U5A--)
- U5 pad 3: Earth -> Net-(U5A-+)
- U6 pad 1: Net-(C19-Pad1) -> Net-(C20-Pad1)
- U7 pad 1: Net-(C17-Pad1) -> MOTOR_01_EN
- U7 pad 10: Net-(U7C-+) -> MOTOR_01_PWM
- U7 pad 11: -5V -> Net-(U7-VCP)
- U7 pad 12: Net-(U7D-+) -> +5V
- U7 pad 13: Net-(U7D--) -> Earth
- U7 pad 14: Net-(D5-A) -> Net-(U7-VINT)
- U7 pad 2: Net-(U7A--) -> MOTOR_01_P
- U7 pad 3: Net-(U7A-+) -> Net-(U7-AISEN)
- U7 pad 4: +5V -> MOTOR_01_N
- U7 pad 5: Net-(U7B-+) -> MOTOR_01_N
- U7 pad 6: Net-(U7B--) -> Net-(U7-AISEN)
- U7 pad 7: Net-(R24-Pad2) -> MOTOR_01_P
- U7 pad 8: Net-(U7D-+) -> MOTOR_01_FAULT
- U7 pad 9: Net-(U7C--) -> MOTOR_01_DIR
- U8 pad 1: +3V3 -> MOTOR_02_EN
- U8 pad 10: ADC_SCL -> MOTOR_02_PWM
- U8 pad 2: ADC_2_ALERT_RDY -> MOTOR_02_P
- U8 pad 3: Earth -> Net-(U8-AISEN)
- U8 pad 4: TRIM_POT_1 -> MOTOR_02_N
- U8 pad 5: TRIM_POT_2 -> MOTOR_02_N
- U8 pad 6: TRIM_POT_3 -> Net-(U8-AISEN)
- U8 pad 7: BTN_1 -> MOTOR_02_P
- U8 pad 8: +3V3 -> MOTOR_02_FAULT
- U8 pad 9: ADC_SDA -> MOTOR_02_DIR
- U9 pad 1: Earth -> MOTOR_03_EN
- U9 pad 10: ADC_SCL -> MOTOR_03_PWM
- U9 pad 2: ADC_1_ALERT_RDY -> MOTOR_03_P
- U9 pad 3: Earth -> Net-(U9-AISEN)
- U9 pad 4: Net-(U9-AIN0) -> MOTOR_03_N
- U9 pad 5: HALL_SENS_01_S -> MOTOR_03_N
- U9 pad 6: HALL_SENS_02_S -> Net-(U9-AISEN)
- U9 pad 7: HALL_SENS_03_S -> MOTOR_03_P
- U9 pad 8: +3V3 -> MOTOR_03_FAULT
- U9 pad 9: ADC_SDA -> MOTOR_03_DIR
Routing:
- net HALL_SENS_01_S: track 0.00 -> 102.9 mm, vias 0 -> 1
- net HALL_SENS_02_S: track 0.00 -> 93.4 mm, vias 0 -> 1
- net HALL_SENS_03_S: track 0.00 -> 84.8 mm, vias 0 -> 1
- net Earth: track 0.00 -> 77.0 mm, vias 0 -> 53
- net +BATT: track 0.00 -> 61.9 mm
- net EMG_01_UC: track 0.00 -> 47.8 mm, vias 0 -> 2
- net +3V3: track 0.00 -> 43.3 mm, vias 0 -> 15
- net UC_BOOT: track 0.00 -> 34.1 mm
- net USB_D+: track 0.00 -> 33.1 mm, vias 0 -> 2
- net USB_D-: track 0.00 -> 31.3 mm, vias 0 -> 4
- net EMG_02_UC: track 0.00 -> 27.5 mm, vias 0 -> 2
- net +5V: track 0.00 -> 27.4 mm, vias 0 -> 19
- net UC_RST: track 0.00 -> 27.3 mm
- net MOTOR_03_P: track 0.00 -> 25.4 mm, vias 0 -> 3
- net TRIM_POT_01: track 0.00 -> 22.8 mm
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- added copper zone on In1.Cu, net +3V3
- added copper zone on F.Cu, net +5V
- added copper zone on In1.Cu, net +5V
- added copper zone on F.Cu, net +BATT
- added copper zone on B.Cu, net Earth
- added copper zone on F.Cu, net Earth
- added copper zone on In2.Cu, net Earth
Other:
- board text added: "1"
- board text added: "2"
- board text added: "3"
- board text added: "4"
- board text added: "BTN"
- board text added: "DIR"
- board text added: "H"
- board text added: "HAPTIC 1"
- board text added: "HAPTIC 2"
- board text added: "HW REV"
- board text added: "JLCJLCJLCJLC"
- board text added: "L"
- board text added: "MOT 1"
- board text added: "MOT 2"
- board text added: "MOT 3"
- board text added: "OpenHand Controller"
- board text added: "PWM"
- board text added: "RX TX"
- board text added: "SDA SCL"
- board text added: "v1.0"
- board text removed: "EMG SENSOR"
- board text removed: "EXTRA UC TEST POINTS TO BE PUT ON BACKSIDE"
- board text removed: "GND RST TDI TDO TCK TMS"
- board text removed: "JTAG"

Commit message: done some routing
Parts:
- moved TP3 2.28 mm to (114.3, 114.9)
- moved TP2 1.92 mm to (114.3, 112.9)
- moved R55 0.74 mm to (198.8, 134.3)
- moved R59 0.74 mm to (206.5, 134.3)
- moved TP34 0.74 mm to (195.2, 134.3)
- moved TP46 0.74 mm to (202.9, 134.3)
- moved TP47 0.74 mm to (206.4, 136.7)
- moved R54 0.64 mm to (191.0, 134.2)
- moved R58 0.64 mm to (178.7, 134.2)
- moved R60 0.64 mm to (183.6, 134.2)
- moved TP32 0.64 mm to (187.5, 134.2)
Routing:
- net MOTOR_03_DIR: track 7.77 -> 119.4 mm, vias 2 -> 3
- net MOTOR_02_DIR: track 0.00 -> 111.2 mm, vias 0 -> 3
- net MOTOR_03_PWM: track 5.89 -> 111.5 mm, vias 2 -> 3
- net MOTOR_02_PWM: track 0.00 -> 102.1 mm, vias 0 -> 3
- net MOTOR_01_DIR: track 0.00 -> 84.6 mm, vias 0 -> 3
- net MOTOR_01_PWM: track 0.00 -> 82.9 mm, vias 0 -> 3
- net -5V: track 4.91 -> 80.5 mm, vias 0 -> 3
- net BTN_01: track 0.00 -> 68.7 mm, vias 0 -> 2
- net HAPTIC_02_DIR: track 0.00 -> 64.4 mm, vias 0 -> 2
- net HAPTIC_02_PWM: track 0.00 -> 61.9 mm, vias 0 -> 2
- net HAPTIC_01_DIR: track 0.00 -> 60.1 mm, vias 0 -> 2
- net HAPTIC_01_PWM: track 0.00 -> 59.5 mm, vias 0 -> 2
- net +3V3: track 43.3 -> 91.6 mm, vias 15 -> 22
- net HAPTIC_01_P: track 0.00 -> 30.3 mm, vias 0 -> 2
- net HAPTIC_01_N: track 0.00 -> 30.0 mm, vias 0 -> 2
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
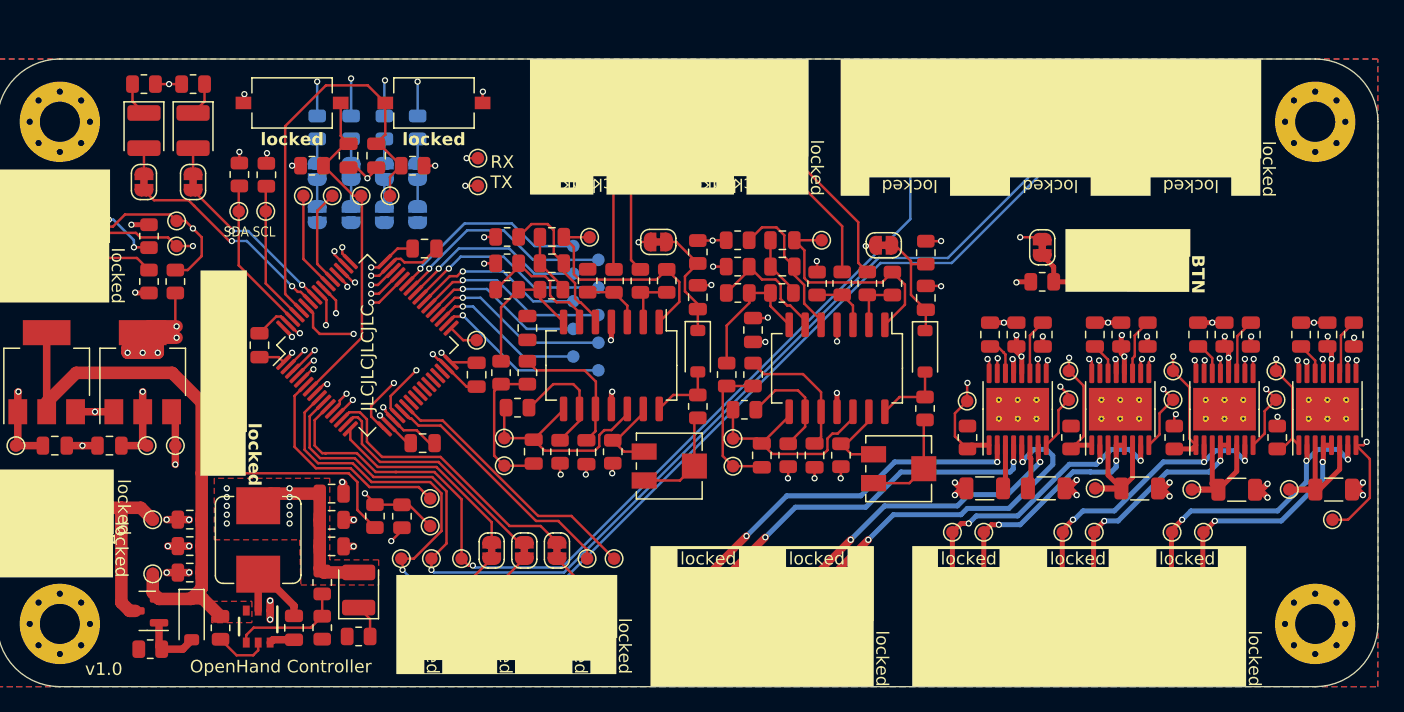
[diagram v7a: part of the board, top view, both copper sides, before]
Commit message: Finish first part of PCB layout and routing
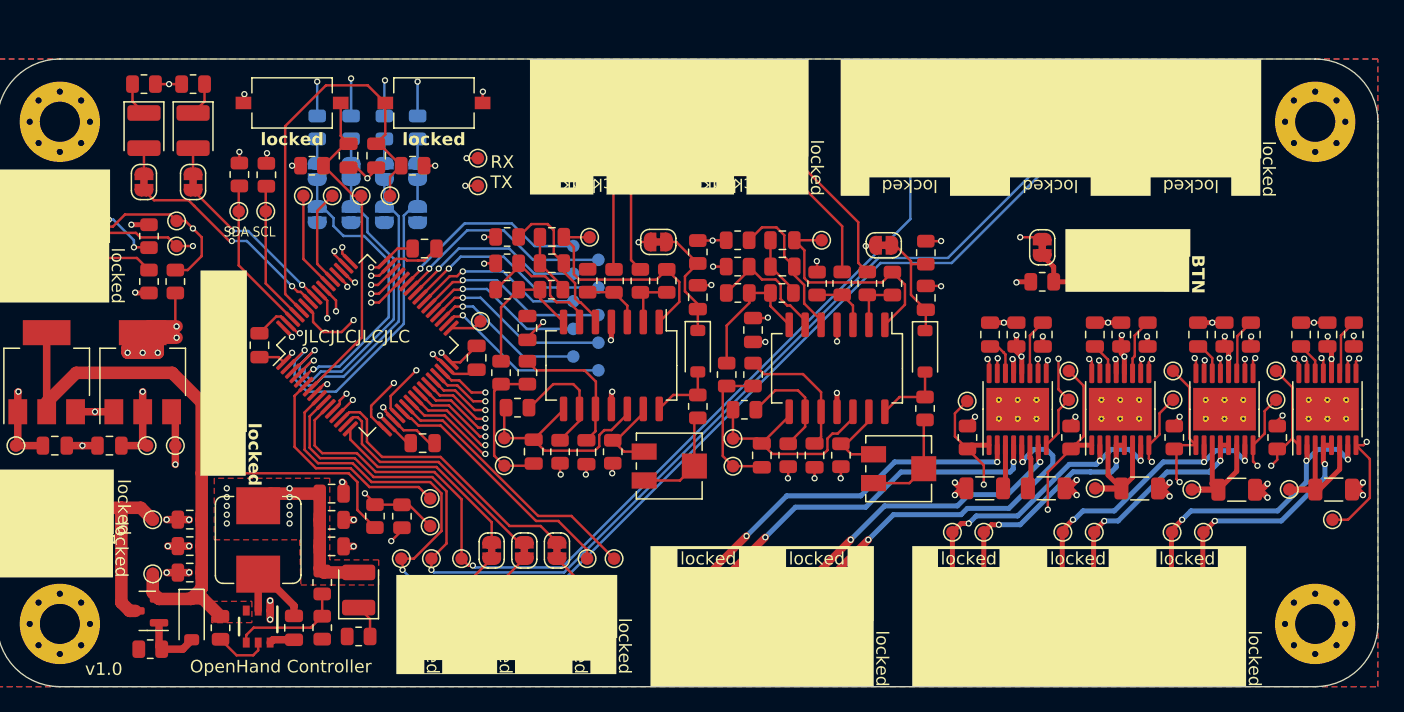
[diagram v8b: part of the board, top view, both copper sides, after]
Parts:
- moved TP18 1.53 mm to (138.5, 120.9)
- moved C4 1.35 mm to (138.2, 123.8)
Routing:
- net MOTOR_03_FAULT: track 9.31 -> 89.3 mm, vias 1 -> 2
- net MOTOR_03_EN: track 9.17 -> 87.5 mm, vias 1 -> 2
- net MOTOR_02_EN: track 9.68 -> 79.8 mm, vias 1 -> 2
- net MOTOR_02_FAULT: track 5.54 -> 75.5 mm, vias 1 -> 2
- net MOTOR_01_FAULT: track 5.58 -> 66.4 mm, vias 1 -> 2
- net MOTOR_01_EN: track 10.0 -> 69.0 mm, vias 1 -> 2
- net HAPTIC_FAULT: track 5.69 -> 58.9 mm, vias 1 -> 2
- net HAPTIC_EN: track 7.94 -> 58.7 mm, vias 1 -> 2
- net HW_REV_01: track 4.01 -> 28.0 mm
- net HW_REV_02: track 4.60 -> 27.4 mm
- net HW_REV_03: track 3.99 -> 25.4 mm
- net HW_REV_04: track 3.45 -> 23.5 mm
- net unconnected-(J5-SHIELD-PadS1): track 0.00 -> 17.0 mm
- net +5V: track 41.8 -> 45.9 mm, vias 30 -> 33
- net MOTOR_03_DIR: track 119.4 -> 120.6 mm
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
